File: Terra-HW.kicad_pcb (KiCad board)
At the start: 4 copper layers, 77 x 68 mm, 97 parts, among them J1 GT-USB-7010ASV, J2 S2B-PH-SM4-TB, J3 0532610271, J5 B8B-PH-SM4-TB, J6 0532610671, Q1 DMP3099L, Q2 2N7002, Q3 2N7002, SW2 KMR231NG, SW3 KMR231NG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

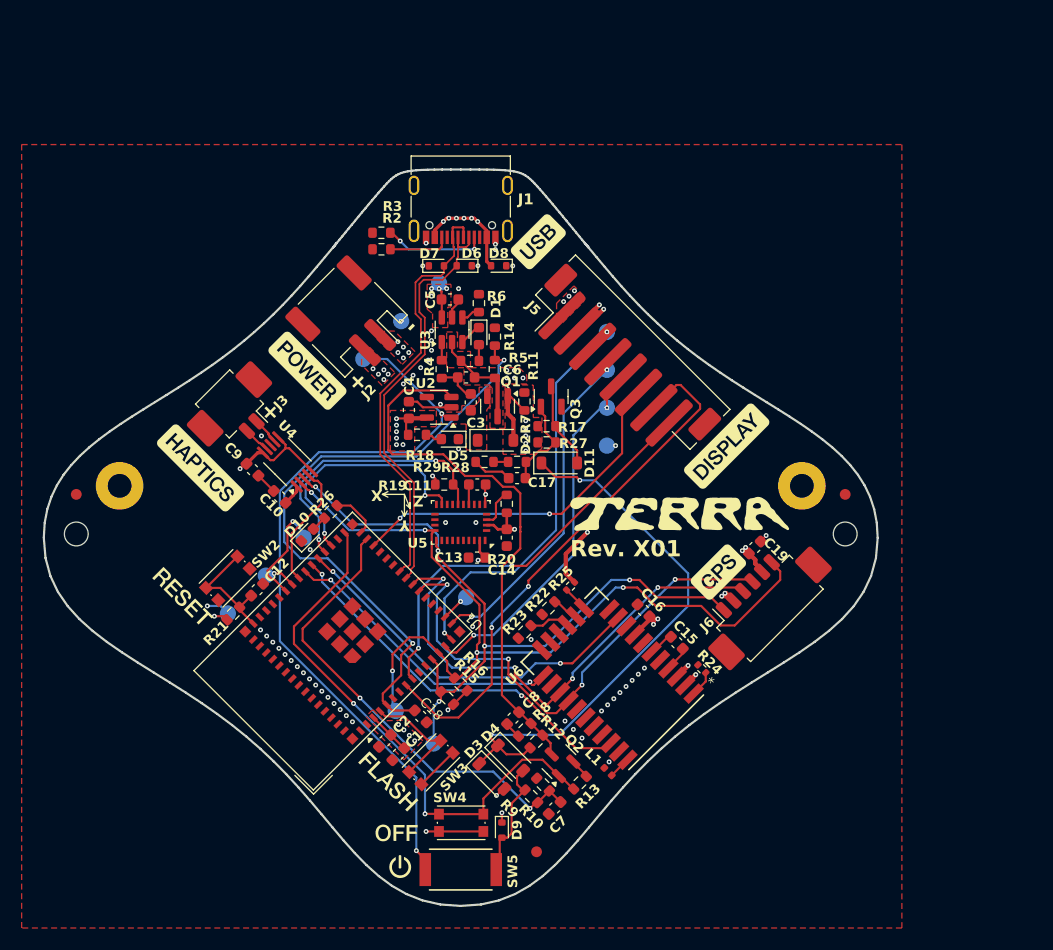
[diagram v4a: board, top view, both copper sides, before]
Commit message: For design review X01-001 Ammendment: Changed ALL VIAS to 0.3/0.55 to reduce fab cost. Signed-off-by: James Mendel <jrm.mendel@gmail.com>
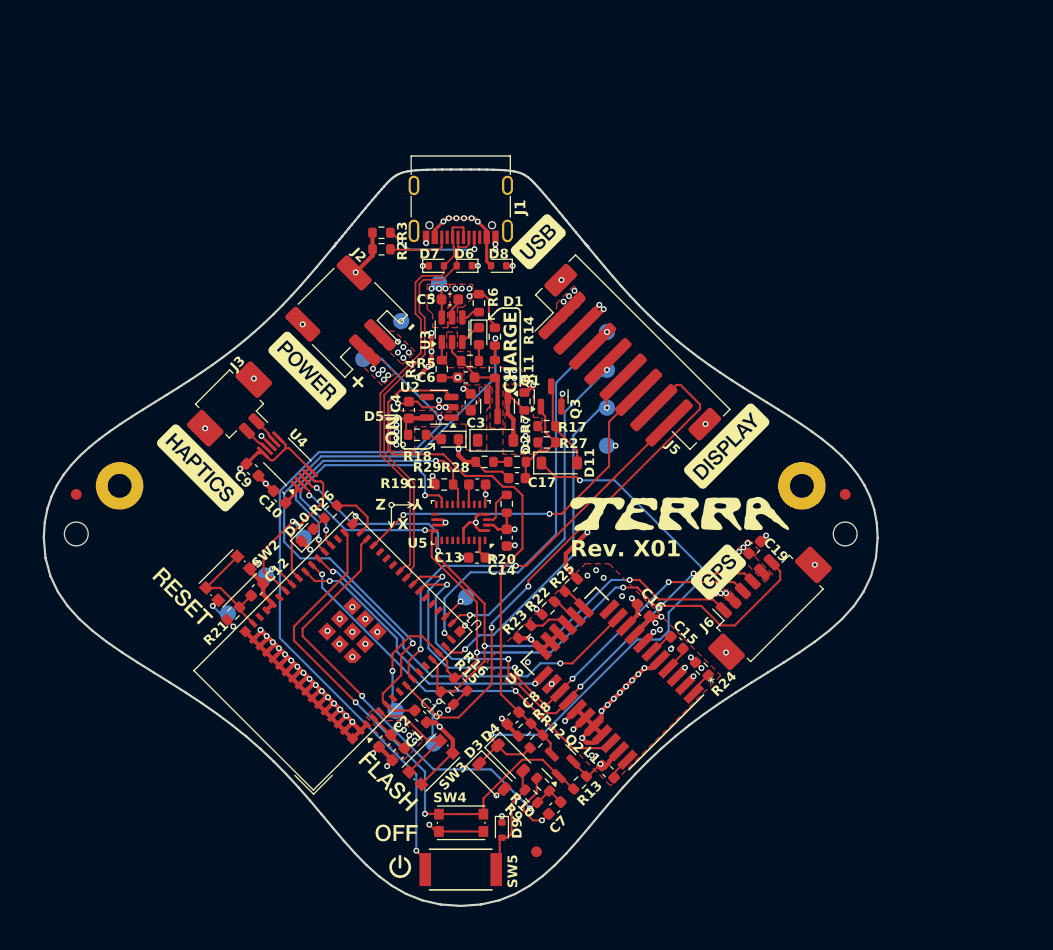
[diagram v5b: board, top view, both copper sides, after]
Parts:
- L1: footprint Inductor_SMD:L_0402_1005Metric -> Inductor_SMD:L_0603_1608Metric
- R24, R25: footprint Resistor_SMD:R_0402_1005Metric -> Resistor_SMD:R_0603_1608Metric
- moved R25 0.09 mm to (160.0, 110.6)
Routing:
- net GND: track 39.3 -> 173.3 mm, vias 66 -> 115
- net +3.3V: track 42.2 -> 39.0 mm, vias 26 -> 27
- net /Microcontroller/VBAT_OVER_2: track 58.1 -> 61.0 mm
- net Net-(D11-K): track 51.3 -> 53.6 mm
- net /Microcontroller/U1RXD: track 45.8 -> 46.5 mm
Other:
- board text added: "CHARGE"
- board text added: "ON"

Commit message: Release X01-003 - Added "JRM" logo to L3 and and Modem Works logo to L4. - Upated copyright - Added alternates for some components - Some cleanup on SCH and PCB.
Signed-off-by: James Mendel <jrm.mendel@gmail.com>
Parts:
- R21: value 5.1k -> 10k
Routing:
- net GND: track 173.3 -> 189.4 mm
- net /Microcontroller/SPI_MOSI: track 37.5 -> 40.6 mm
- net /Microcontroller/SPI_SCK: track 31.7 -> 34.4 mm
- net /Microcontroller/SPI_~{CS0_DISP}: track 31.8 -> 33.1 mm
- net +3.3V: track 39.0 -> 40.2 mm
- net /Microcontroller/PWROFF: track 50.7 -> 51.6 mm

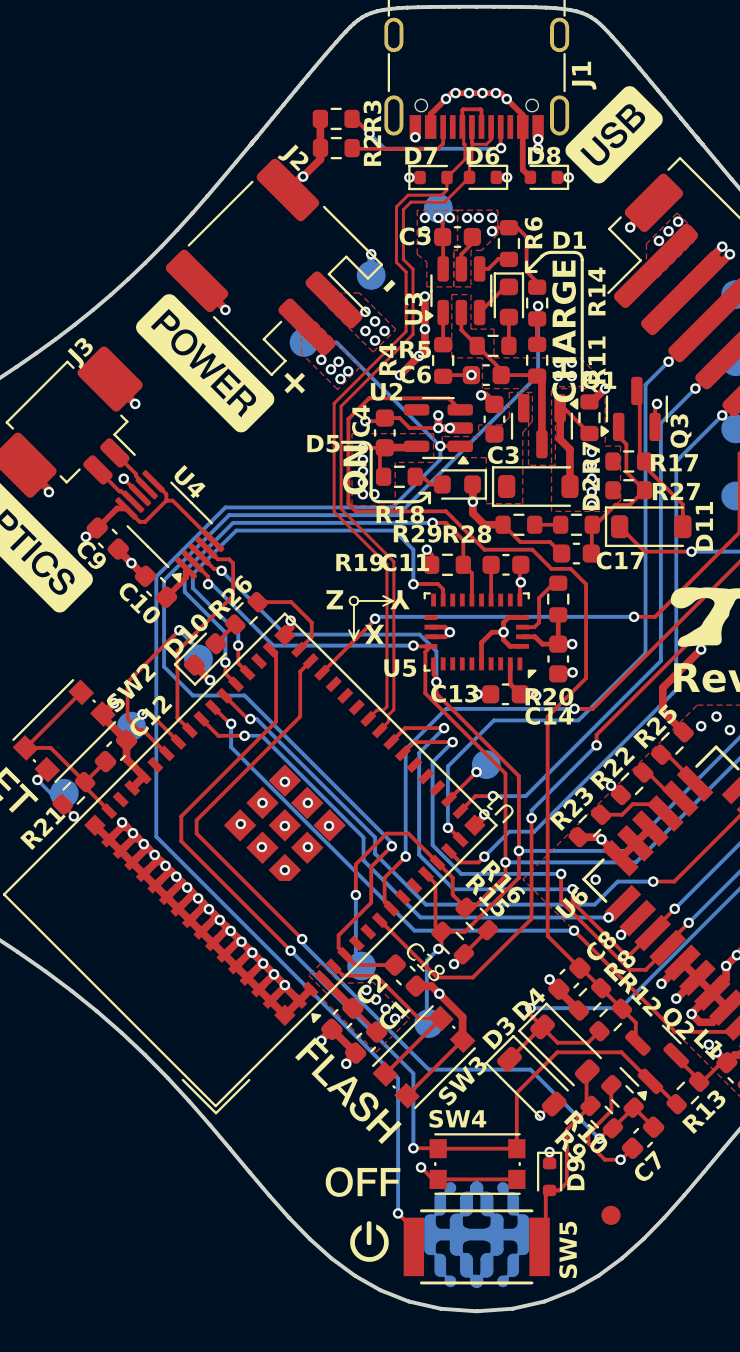
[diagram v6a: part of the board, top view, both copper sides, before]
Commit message: Release X01-004 - Reduced size of 0.3mm pad / 0.2mm pitch to increase pitch to >0.22mm - Removed via-in-pad
Signed-off-by: James Mendel <jrm.mendel@gmail.com>
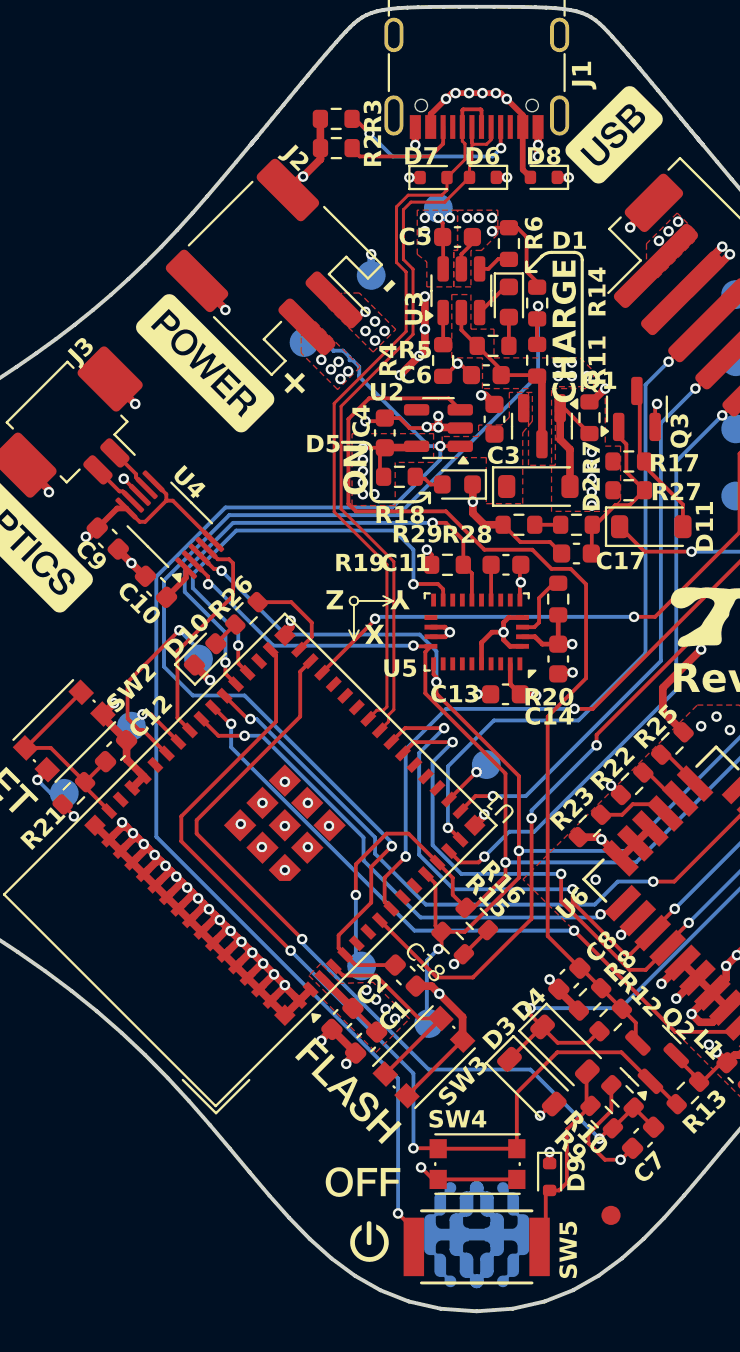
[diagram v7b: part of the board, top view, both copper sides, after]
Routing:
- net GND: track 189.4 -> 192.8 mm
